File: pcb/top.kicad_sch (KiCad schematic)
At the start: 63 parts, among them J1 Conn_01x01, J10 Conn_01x01, J11 Conn_01x01, J2 Conn_01x01, J3 Conn_01x06, J4 Conn_01x01, J5 Conn_01x01, J6 Conn_01x01, J7 Conn_01x01, J8 Conn_01x01, J9 Conn_01x01, Q1 2N7002, Q2 2N7002, Q3 2N7002, Q4 2N7002, U1 L78L05_SOT89, U2 PIC12F629-ISN

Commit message: Add OSHW logo.
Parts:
- Q1, Q2, Q3, Q4: JLCPCB_CORRECTION (none) -> 0;0;180
- R10, R12, R13, R14, R7: LCSC C17407 -> C149504
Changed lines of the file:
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@@
+      (effects (font (size 1.27 1.27)) hide)
+    )
+    (property "JLCPCB_CORRECTION" "0;0;180" (id 5) (at 217.17 135.89 0)
       (effects (font (size 1.27 1.27)) hide)
     )
@@
       (effects (font (size 1.27 1.27)) hide)
     )
-    (property "LCSC" "C17407" (id 4) (at 137.16 120.65 0)
+    (property "LCSC" "C149504" (id 4) (at 137.16 120.65 0)
       (effects (font (size 1.27 1.27)) hide)
     )
@@
       (effects (font (size 1.27 1.27)) hide)
     )
-    (property "LCSC" "C17407" (id 4) (at 209.55 139.7 0)
+    (property "LCSC" "C149504" (id 4) (at 209.55 139.7 0)
       (effects (font (size 1.27 1.27)) hide)
     )
@@
       (effects (font (size 1.27 1.27)) hide)
     )
+    (property "JLCPCB_CORRECTION" "0;0;180" (id 5) (at 242.57 128.27 0)
+      (effects (font (size 1.27 1.27)) hide)
+    )
     (pin "1")
     (pin "2")
@@
       (effects (font (size 1.27 1.27)) hide)
     )
-    (property "LCSC" "C17407" (id 4) (at 234.95 132.08 0)
+    (property "LCSC" "C149504" (id 4) (at 234.95 132.08 0)
       (effects (font (size 1.27 1.27)) hide)
     )
@@
       (effects (font (size 1.27 1.27)) hide)
     )
+    (property "JLCPCB_CORRECTION" "0;0;180" (id 5) (at 102.87 138.43 0)
+      (effects (font (size 1.27 1.27)) hide)
+    )
     (pin "1")
     (pin "2")
@@
       (effects (font (size 1.27 1.27)) hide)
     )
-    (property "LCSC" "C17407" (id 4) (at 110.49 142.24 0)
+    (property "LCSC" "C149504" (id 4) (at 110.49 142.24 0)
       (effects (font (size 1.27 1.27)) hide)
     )
@@
       (effects (font (size 1.27 1.27)) hide)
     )
+    (property "JLCPCB_CORRECTION" "0;0;180" (id 5) (at 72.39 135.89 0)
+      (effects (font (size 1.27 1.27)) hide)
+    )
     (pin "1")
     (pin "2")
@@
       (effects (font (size 1.27 1.27)) hide)
     )
-    (property "LCSC" "C17407" (id 4) (at 80.01 139.7 0)
-      (effects (font (size 1.27 1.27)) hide)
-    )
+    (property "LCSC" "C149504" (id 4) (at 80.01 139.7 0)
+      (effects (font (size 1.27 1.27)) hide)
+    )

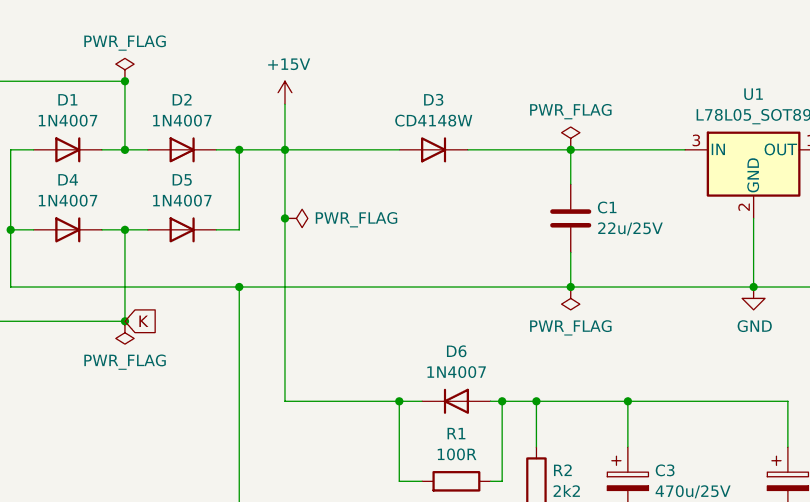
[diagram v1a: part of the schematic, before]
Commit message: Top: add 100n capacitor on input.
To filter DCC edges (causing transistors to open).
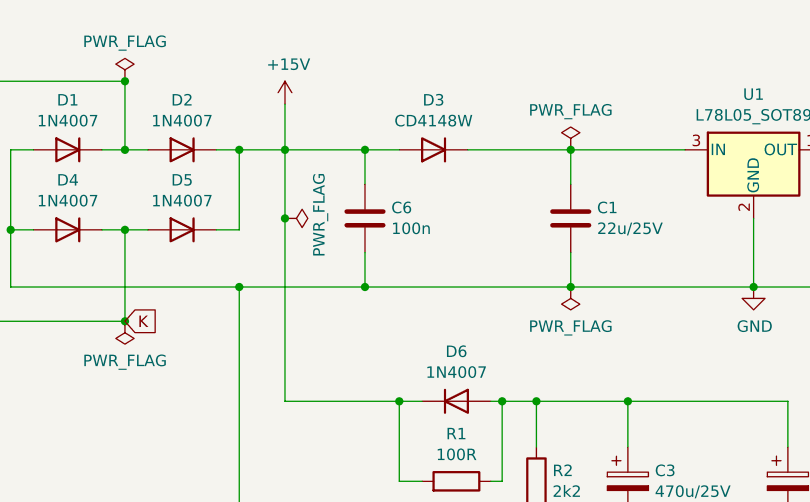
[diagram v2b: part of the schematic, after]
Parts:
- added C6: 100n, Capacitor_SMD:C_0805_2012Metric_Pad1.18x1.45mm_HandSolder, symbol Device:C
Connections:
- net +15V: now also C6.1
- net GND: now also C6.2
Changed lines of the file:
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@@
     (title "Osvětlení vozů Balm MTB model - horní deska")
     (date "2021-12-23")
-    (rev "1.0")
+    (rev "1.1")
     (company "Model Railroader Club Brno I – KMŽ Brno I – https://kmz-brno.cz/")
     (comment 1 "Jan Horáček; inspirováno https://usuaris.tinet.cat/fmco/dccfunc_en.html")
@@
   (junction (at 115.57 36.83) (diameter 0) (color 0 0 0 0)
   )
+  (junction (at 92.71 52.07) (diameter 0) (color 0 0 0 0)
+  )
   (junction (at 66.04 36.83) (diameter 0) (color 0 0 0 0)
   )
   (junction (at 83.82 44.45) (diameter 0) (color 0 0 0 0)
+  )
+  (junction (at 92.71 36.83) (diameter 0) (color 0 0 0 0)
   )
   (junction (at 135.89 52.07) (diameter 0) (color 0 0 0 0)
@@
     (stroke (width 0) (type default) (color 0 0 0 0))
   )
-  (wire (pts (xy 83.82 36.83) (xy 96.52 36.83))
+  (wire (pts (xy 83.82 36.83) (xy 92.71 36.83))
     (stroke (width 0) (type default) (color 0 0 0 0))
   )
@@
     (stroke (width 0) (type default) (color 0 0 0 0))
   )
+  (wire (pts (xy 92.71 48.26) (xy 92.71 52.07))
+    (stroke (width 0) (type default) (color 0 0 0 0))
+  )
   (wire (pts (xy 152.4 113.03) (xy 152.4 116.84))
     (stroke (width 0) (type default) (color 0 0 0 0))
@@
     (stroke (width 0) (type default) (color 0 0 0 0))
   )
+  (wire (pts (xy 92.71 36.83) (xy 96.52 36.83))
+    (stroke (width 0) (type default) (color 0 0 0 0))
+  )
   (wire (pts (xy 44.45 63.5) (xy 44.45 59.69))
     (stroke (width 0) (type default) (color 0 0 0 0))
@@
     (stroke (width 0) (type default) (color 0 0 0 0))
   )
+  (wire (pts (xy 92.71 52.07) (xy 115.57 52.07))
+    (stroke (width 0) (type default) (color 0 0 0 0))
+  )
   (wire (pts (xy 219.71 73.66) (xy 224.79 73.66))
     (stroke (width 0) (type default) (color 0 0 0 0))
@@
     (stroke (width 0) (type default) (color 0 0 0 0))
   )
-  (wire (pts (xy 78.74 52.07) (xy 115.57 52.07))
+  (wire (pts (xy 78.74 52.07) (xy 92.71 52.07))
     (stroke (width 0) (type default) (color 0 0 0 0))
   )
@@
   )
   (wire (pts (xy 78.74 45.72) (xy 78.74 36.83))
+    (stroke (width 0) (type default) (color 0 0 0 0))
+  )
+  (wire (pts (xy 92.71 36.83) (xy 92.71 40.64))
     (stroke (width 0) (type default) (color 0 0 0 0))
   )
@@
       (effects (font (size 1.27 1.27)) hide)
     )
-    (property "Value" "PWR_FLAG" (id 1) (at 87.0712 44.45 90)
+    (property "Value" "PWR_FLAG" (id 1) (at 87.63 39.37 0)
       (effects (font (size 1.27 1.27)) (justify left))
     )
@@
     (pin "2")
   )
+  (symbol (lib_id "Device:C") (at 92.71 44.45 0) (unit 1)
+    (in_bom yes) (on_board yes)
+    (property "Reference" "C6" (id 0) (at 95.631 43.2816 0)
+      (effects (font (size 1.27 1.27)) (justify left))
+    )
+    (property "Value" "100n" (id 1) (at 95.631 45.593 0)
+      (effects (font (size 1.27 1.27)) (justify left))
+    )
+    (property "Footprint" "Capacitor_SMD:C_0805_2012Metric_Pad1.18x1.45mm_HandSolder" (id 2) (at 93.6752 48.26 0)
+      (effects (font (size 1.27 1.27)) hide)
+    )
+    (property "Datasheet" "~" (id 3) (at 92.71 44.45 0)
+      (effects (font (size 1.27 1.27)) hide)
+    )
+    (property "LCSC" "C49678" (id 4) (at 92.71 44.45 0)
+      (effects (font (size 1.27 1.27)) hide)
+    )
+    (pin "1")
+    (pin "2")
+  )
   (sheet_instances
     (path "/" (page "1"))
@@
       (reference "C5") (unit 1) (value "1000u/25V") (footprint "Capacitor_THT:CP_Radial_D10.0mm_P5.00mm")
     )
+    (path "/0e4fe764-47ff-46fb-a357-7161a110fc25"
+      (reference "C6") (unit 1) (value "100n") (footprint "Capacitor_SMD:C_0805_2012Metric_Pad1.18x1.45mm_HandSolder")
+    )
     (path "/00000000-0000-0000-0000-000061c6e829"

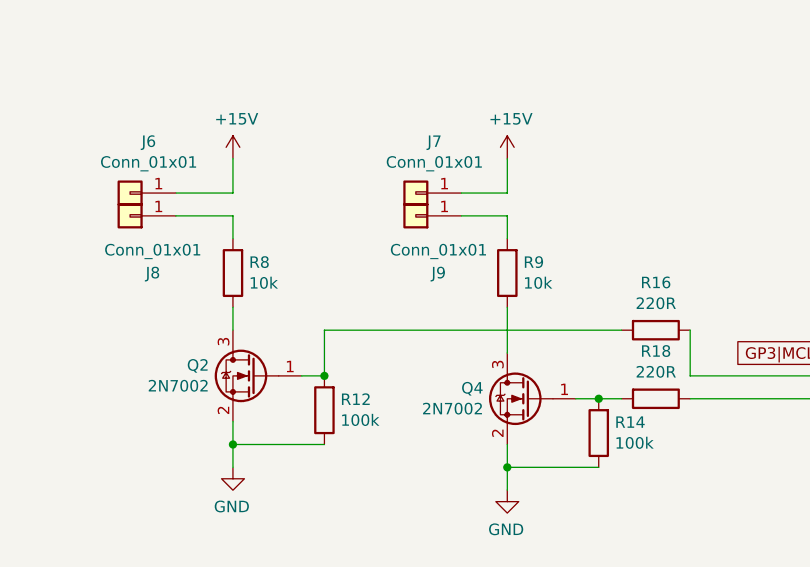
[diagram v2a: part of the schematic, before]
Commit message: Change front transistors 10k → 47k.
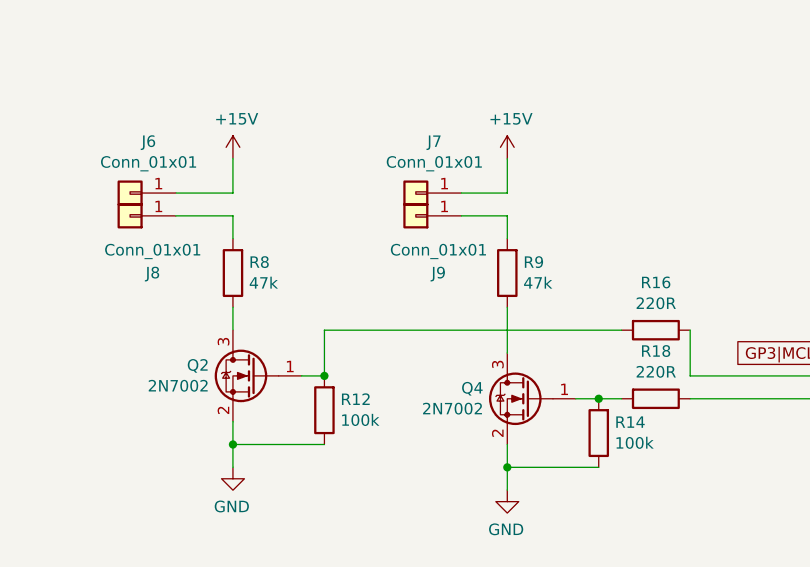
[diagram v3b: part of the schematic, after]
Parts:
- R8, R9: value 10k -> 47k; LCSC C17414 -> C17713
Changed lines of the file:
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@@
       (effects (font (size 1.27 1.27)) (justify right))
     )
-    (property "Value" "10k" (id 1) (at 102.108 125.603 0)
+    (property "Value" "47k" (id 1) (at 102.108 125.603 0)
       (effects (font (size 1.27 1.27)) (justify right))
     )
@@
       (effects (font (size 1.27 1.27)) hide)
     )
-    (property "LCSC" "C17414" (id 4) (at 100.33 124.46 0)
+    (property "LCSC" "C17713" (id 4) (at 100.33 124.46 0)
       (effects (font (size 1.27 1.27)) hide)
     )
@@
       (effects (font (size 1.27 1.27)) (justify right))
     )
-    (property "Value" "10k" (id 1) (at 71.628 125.603 0)
+    (property "Value" "47k" (id 1) (at 71.628 125.603 0)
       (effects (font (size 1.27 1.27)) (justify right))
     )
@@
       (effects (font (size 1.27 1.27)) hide)
     )
-    (property "LCSC" "C17414" (id 4) (at 69.85 124.46 0)
+    (property "LCSC" "C17713" (id 4) (at 69.85 124.46 0)
       (effects (font (size 1.27 1.27)) hide)
     )
@@
     )
     (path "/00000000-0000-0000-0000-000061e57dfe"
-      (reference "R8") (unit 1) (value "10k") (footprint "Resistor_SMD:R_0805_2012Metric_Pad1.20x1.40mm_HandSolder")
+      (reference "R8") (unit 1) (value "47k") (footprint "Resistor_SMD:R_0805_2012Metric_Pad1.20x1.40mm_HandSolder")
     )
     (path "/00000000-0000-0000-0000-000061e4f7a3"
-      (reference "R9") (unit 1) (value "10k") (footprint "Resistor_SMD:R_0805_2012Metric_Pad1.20x1.40mm_HandSolder")
+      (reference "R9") (unit 1) (value "47k") (footprint "Resistor_SMD:R_0805_2012Metric_Pad1.20x1.40mm_HandSolder")
     )
     (path "/00000000-0000-0000-0000-000061d26723"

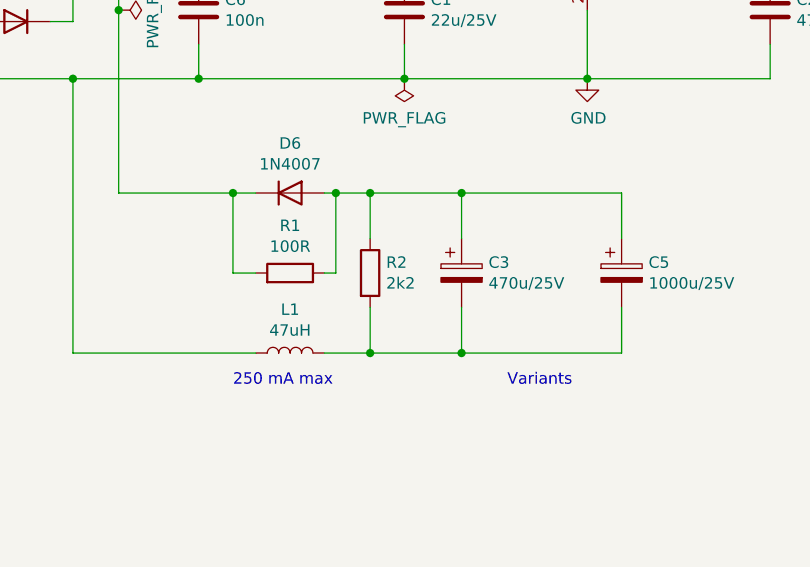
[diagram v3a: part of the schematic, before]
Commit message: Change capacitor-discharge resistor to 22k.
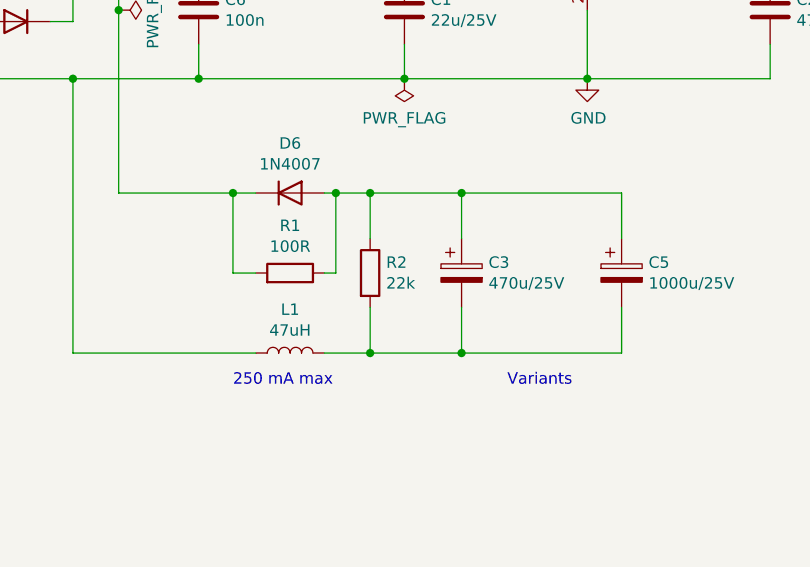
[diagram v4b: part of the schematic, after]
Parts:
- R2: value 2k2 -> 22k; LCSC C17520 -> C17560
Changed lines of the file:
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@@
       (effects (font (size 1.27 1.27)) (justify left))
     )
-    (property "Value" "2k2" (id 1) (at 113.538 74.803 0)
+    (property "Value" "22k" (id 1) (at 113.538 74.803 0)
       (effects (font (size 1.27 1.27)) (justify left))
     )
@@
       (effects (font (size 1.27 1.27)) hide)
     )
-    (property "LCSC" "C17520" (id 4) (at 111.76 73.66 0)
+    (property "LCSC" "C17560" (id 4) (at 111.76 73.66 0)
       (effects (font (size 1.27 1.27)) hide)
     )
@@
     )
     (path "/00000000-0000-0000-0000-000061eef049"
-      (reference "R2") (unit 1) (value "2k2") (footprint "Resistor_SMD:R_0805_2012Metric_Pad1.20x1.40mm_HandSolder")
+      (reference "R2") (unit 1) (value "22k") (footprint "Resistor_SMD:R_0805_2012Metric_Pad1.20x1.40mm_HandSolder")
     )
     (path "/00000000-0000-0000-0000-000061c84938"
